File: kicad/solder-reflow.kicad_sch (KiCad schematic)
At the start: 37 parts, among them J1 XT60PW-M, J2 1985807, J3 Conn_01x06_Male, U1 ESP32-WROOM-32E-N8, U2 DGD0215WT-7, U3 AP62201WU-7, U4 MAX31855KASA+T

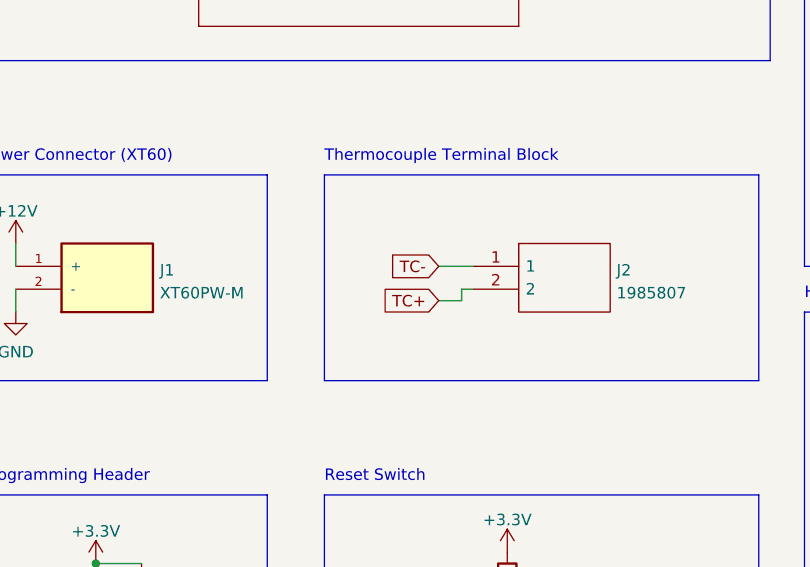
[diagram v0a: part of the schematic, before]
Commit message: Tweaked layout; refined buck layout; added graphics
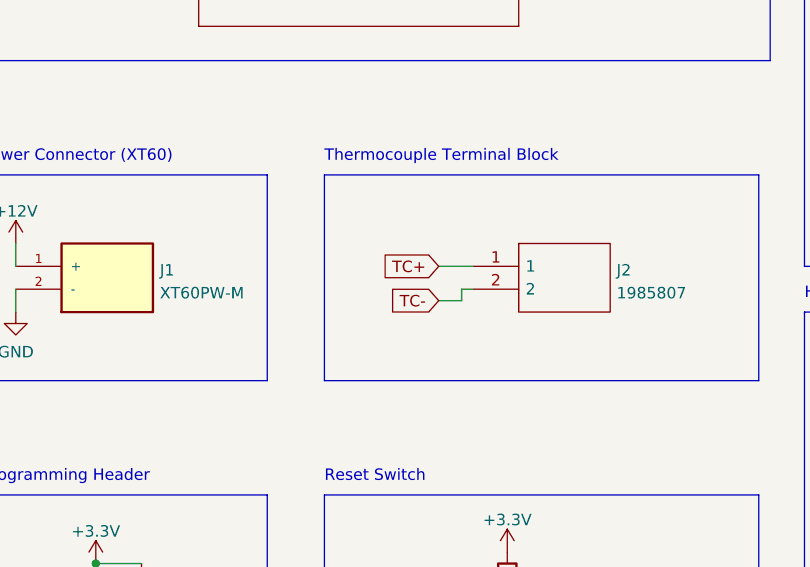
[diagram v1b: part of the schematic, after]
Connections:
- net TC+: now also J2.1; no longer J2.2
- net TC-: now also J2.2; no longer J2.1
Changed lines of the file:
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@@
     )
   )
-  (global_label "TC+" (shape input) (at 73.66 128.27 180) (fields_autoplaced)
+  (global_label "TC-" (shape input) (at 73.66 128.27 180) (fields_autoplaced)
     (effects (font (size 1.27 1.27)) (justify right))
-    (property "Intersheet References" "${INTERSHEET_REFS}" (id 0) (at 67.4369 128.3494 0)
+    (property "Intersheet References" "${INTERSHEET_REFS}" (id 0) (at 67.4369 128.1906 0)
       (effects (font (size 1.27 1.27)) (justify right) hide)
     )
   )
-  (global_label "TC-" (shape input) (at 73.66 124.46 180) (fields_autoplaced)
+  (global_label "TC+" (shape input) (at 73.66 124.46 180) (fields_autoplaced)
     (effects (font (size 1.27 1.27)) (justify right))
-    (property "Intersheet References" "${INTERSHEET_REFS}" (id 0) (at 67.4369 124.5394 0)
+    (property "Intersheet References" "${INTERSHEET_REFS}" (id 0) (at 67.4369 124.3806 0)
       (effects (font (size 1.27 1.27)) (justify right) hide)
     )

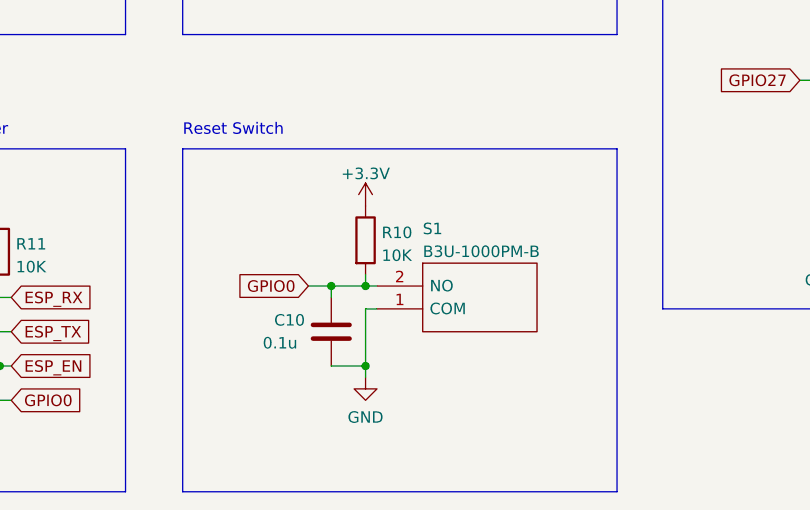
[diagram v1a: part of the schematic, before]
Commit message: Changed tactile switch part
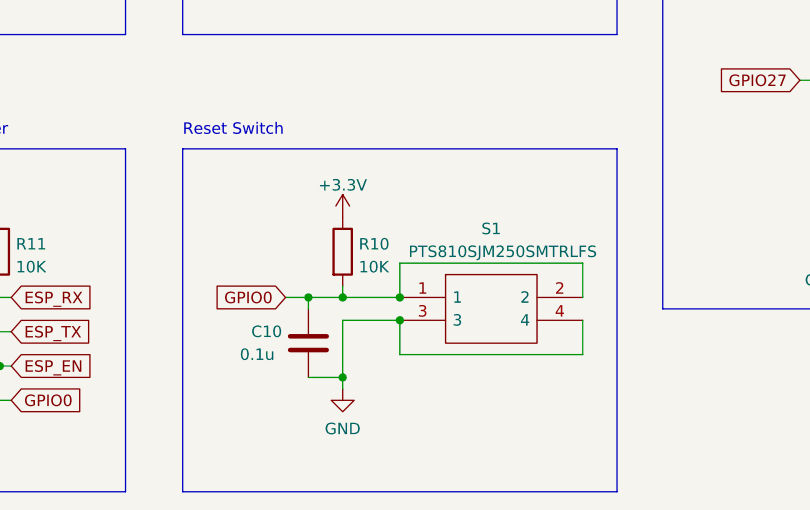
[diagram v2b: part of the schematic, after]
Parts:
- removed S1: B3U-1000PM-B, mouser_ecad:B3U1000PMB, symbol B3U-1000PM-B:B3U-1000PM-B
- added S1: PTS810SJM250SMTRLFS, mouser_ecad:PTS810SJG250SMTRLFS, symbol PTS810SJM250SMTRLFS:PTS810SJM250SMTRLFS
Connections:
- net GND: now also S1.3, S1.4
- net GPIO0: now also S1.1, S1.2
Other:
- moved on the sheet: C10, R10
